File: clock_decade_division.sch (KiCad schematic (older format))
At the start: 17 parts, among them SW1 SW_Rotary12, U1 74LVC161, U2 74LVC161, U3 74LVC161, U4 74LVC161, U5 74LVC00, U6 74LVC161, U7 74LVC161, U8 74LVC00

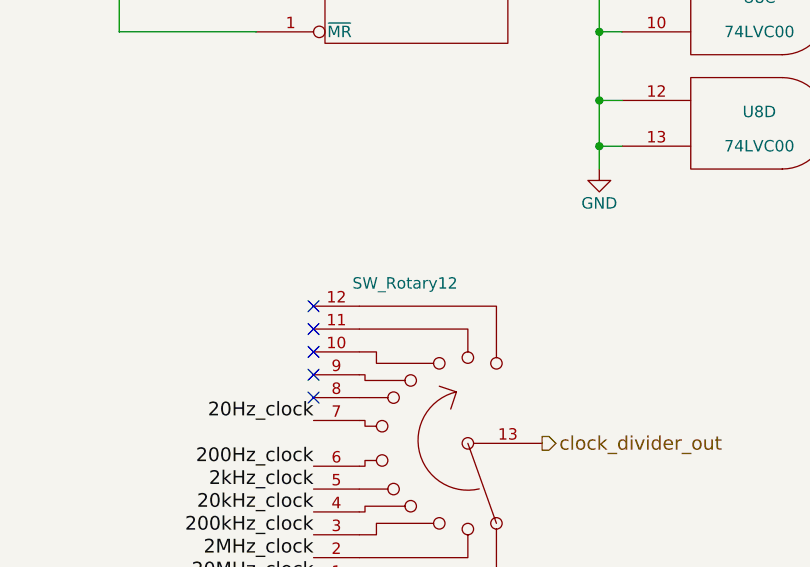
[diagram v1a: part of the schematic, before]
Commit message: R2 PCB rotary switches closer to middle of board
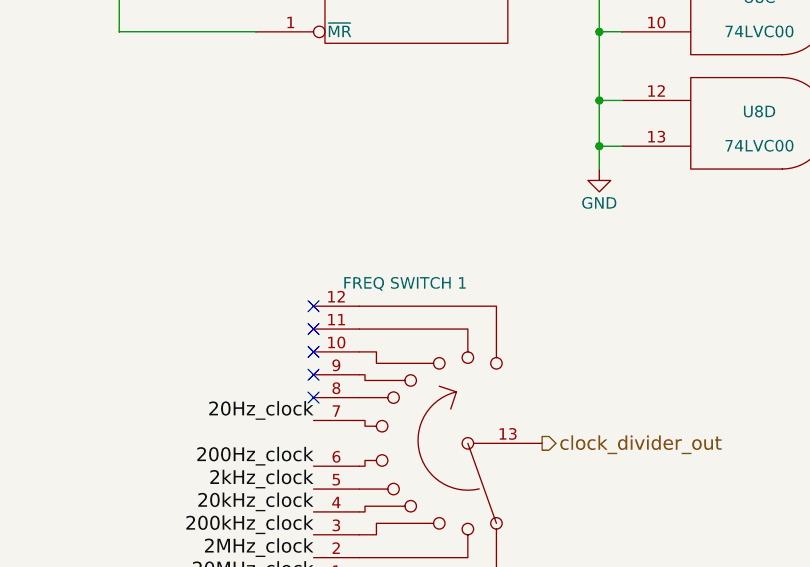
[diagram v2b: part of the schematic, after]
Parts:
- SW1: value SW_Rotary12 -> FREQ SWITCH 1; Distributor (none) -> Mouser; Distributor PN (none) -> 633-MRK112A; Manufacturer (none) -> NKK; Manufacturer PN (none) -> MRK112-A; URL (none) -> http://www.mouser.com/Search/ProductDetail.aspx?R=MRK112-Av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; Unit Price (none) -> 11.80
- U1, U2, U3, U4, U6, U7: Distributor (none) -> Mouser; Distributor PN (none) -> 771-LVC161D118; Manufacturer (none) -> Nexperia; Manufacturer PN (none) -> 4LVC161D118; URL (none) -> http://www.mouser.com/Search/ProductDetail.aspx?R=74LVC161D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; Unit Price (none) -> 0.61
- U5, U8: Distributor (none) -> Mouser; Distributor PN (none) -> 595-SN74LVC00ADR; Manufacturer (none) -> TI; Manufacturer PN (none) -> SN74LVC00ADR; URL (none) -> http://www.mouser.com/Search/ProductDetail.aspx?R=SN74LVC00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; Unit Price (none) -> 0.40

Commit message: update switch models in library, rotate final clock division switch
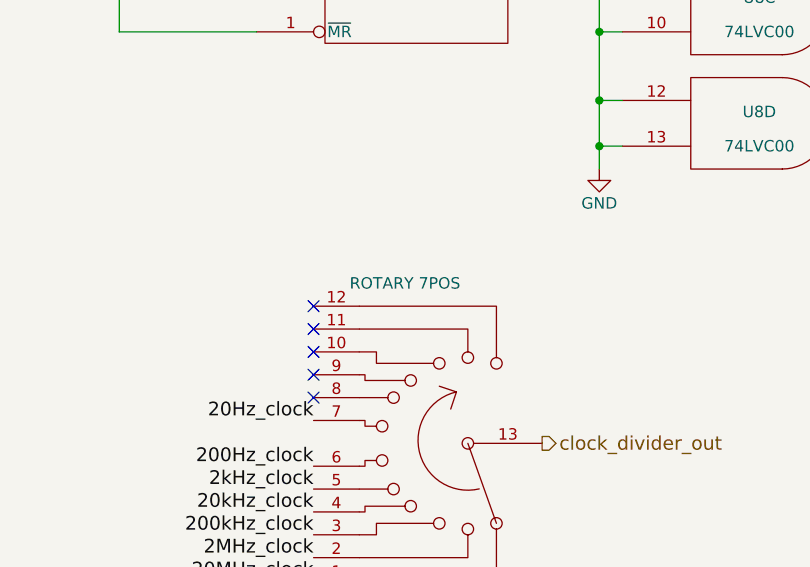
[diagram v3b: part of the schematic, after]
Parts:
- SW1: value FREQ SWITCH 1 -> ROTARY 7POS
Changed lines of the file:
@@
 P 7950 5400
 F 0 "SW1" H 7950 6100 50  0000 C CNN
-F 1 "FREQ SWITCH 1" H 7950 4700 50  0000 C CNN
+F 1 "ROTARY 7POS" H 7950 4700 50  0000 C CNN
 F 2 "calbox:SW_ROTARY_SP12T_MRK112" H 7750 6100 50  0001 C CNN
 F 3 "http://www.mouser.com/ds/2/295/MRlogicLevel-9701.pdf" H 7750 6100 50  0001 C CNN
